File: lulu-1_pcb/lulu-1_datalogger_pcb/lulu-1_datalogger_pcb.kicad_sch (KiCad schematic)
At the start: 38 parts, among them J1 B2B-XH-A, J2 SBH11-PBPC-D10-ST-BK, J3 MEM2067-02-180-00-A_REVB, SW1 SW_Nidec_CAS-120A1, U1 STM32F401RETx, U2 BAT54LT1G, U3 LP3982ILD-3.3, U4 BMP280, U5 MPU-6050, U6 W25Q16JVSS, Y1 25 Mhz, Y2 32 Khz

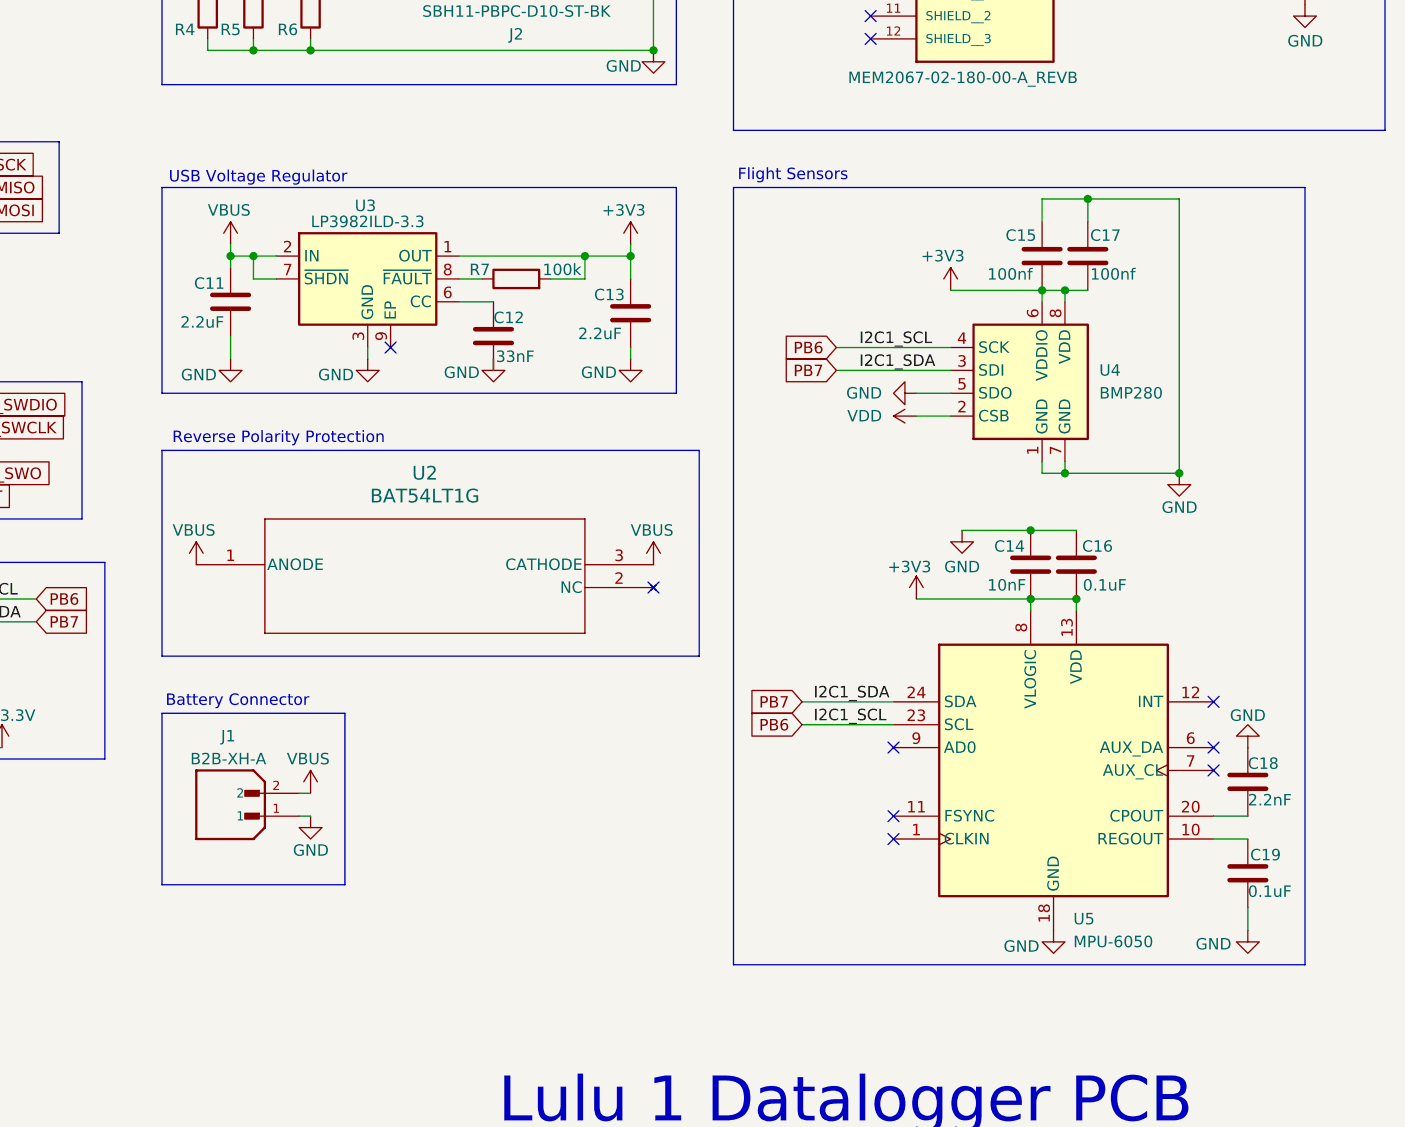
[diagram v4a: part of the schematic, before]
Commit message: added continuity LED to voltage regulator output
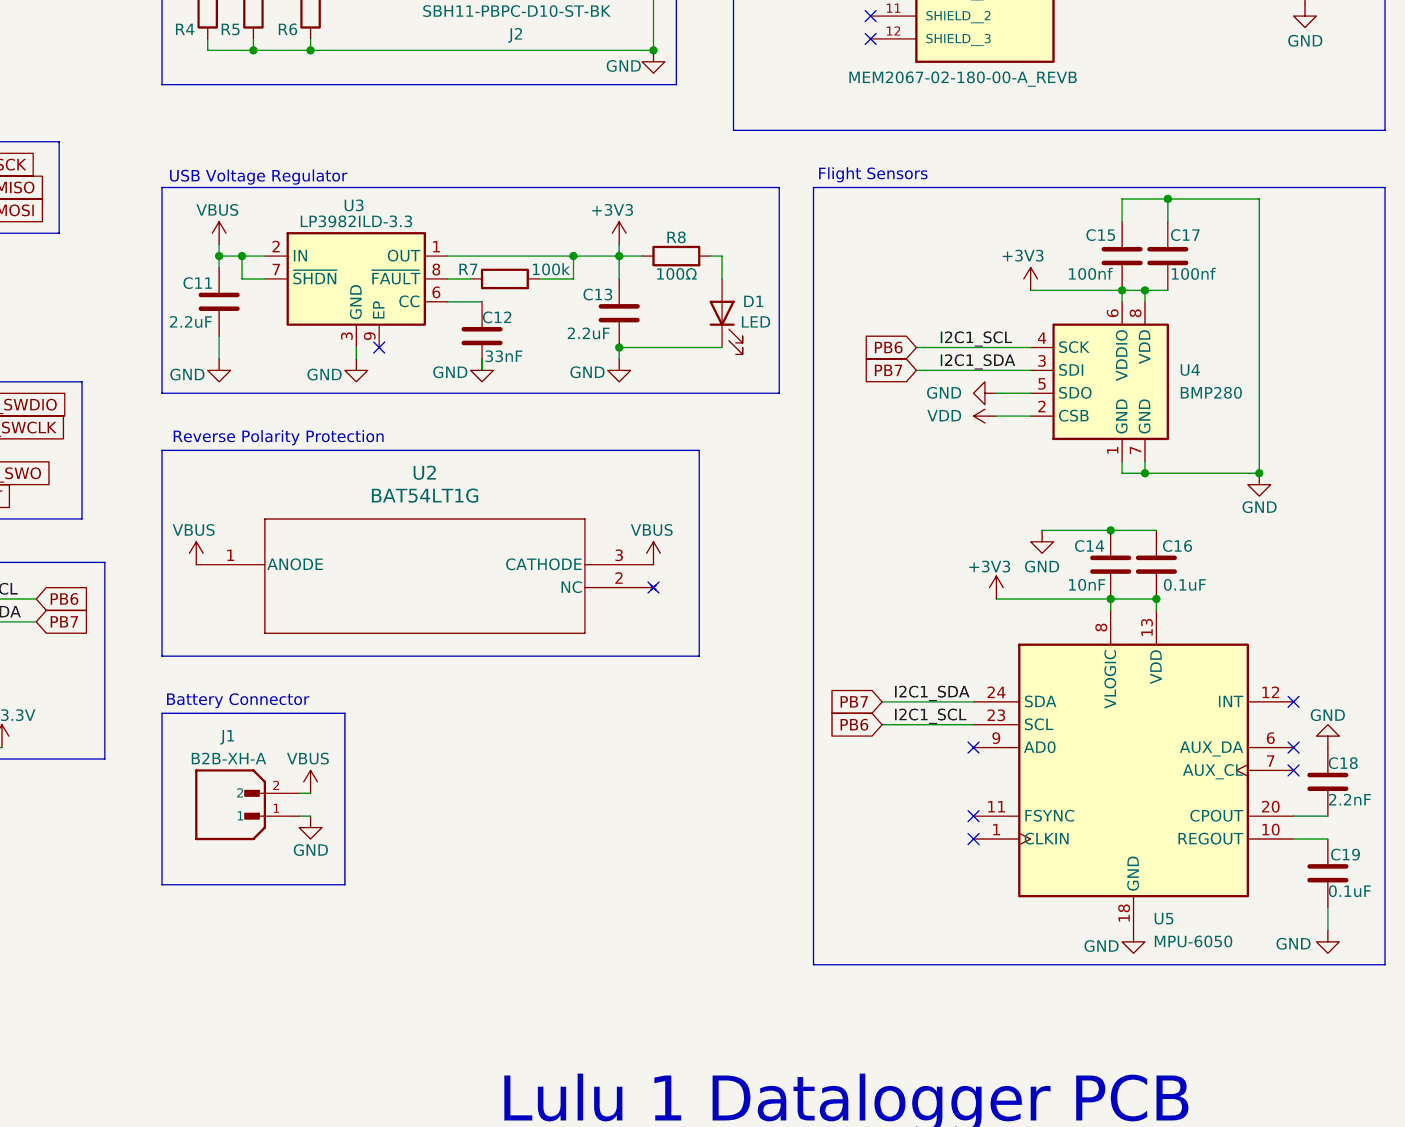
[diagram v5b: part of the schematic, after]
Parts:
- added D1: LED, symbol Device:LED
- added R8: 100Ω, symbol Device:R
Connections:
- net +3V3: now also R8.1
- net GND: now also D1.1 (K)
- new net: D1.2 (A), R8.2
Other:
- moved on the sheet: C11, C12, C13, C14, C15, C16, C17, C18, C19, R7, U3, U4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

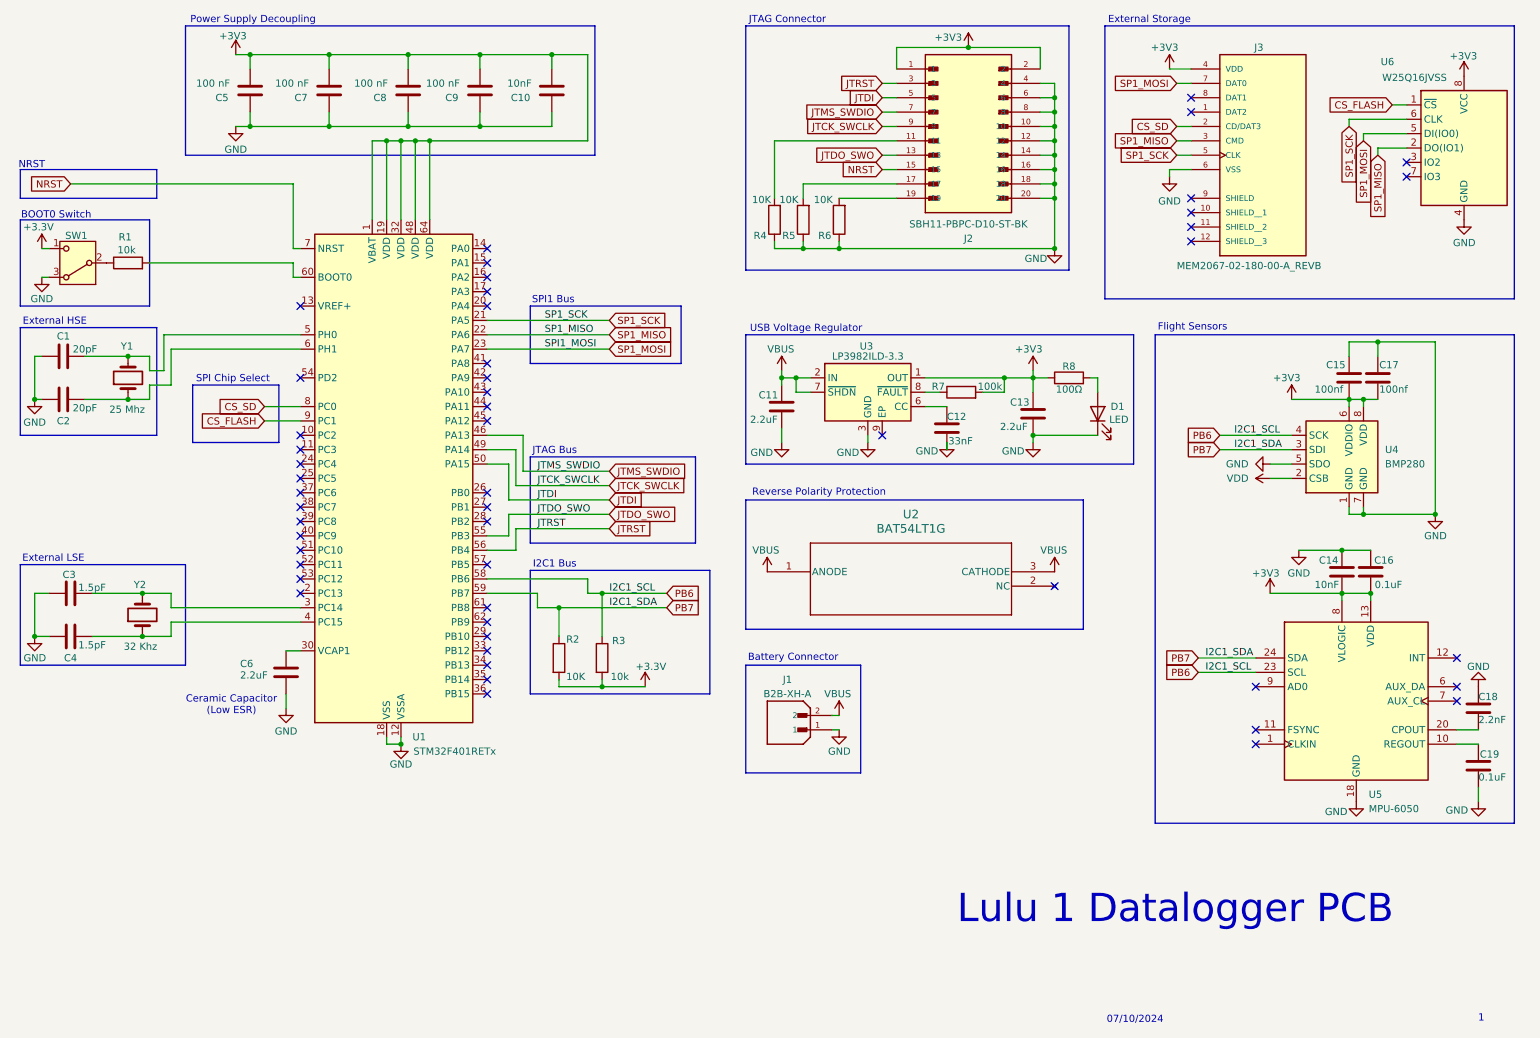
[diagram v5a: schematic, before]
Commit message: added programmable LEDs and buzzer to schematic and to .ioc file
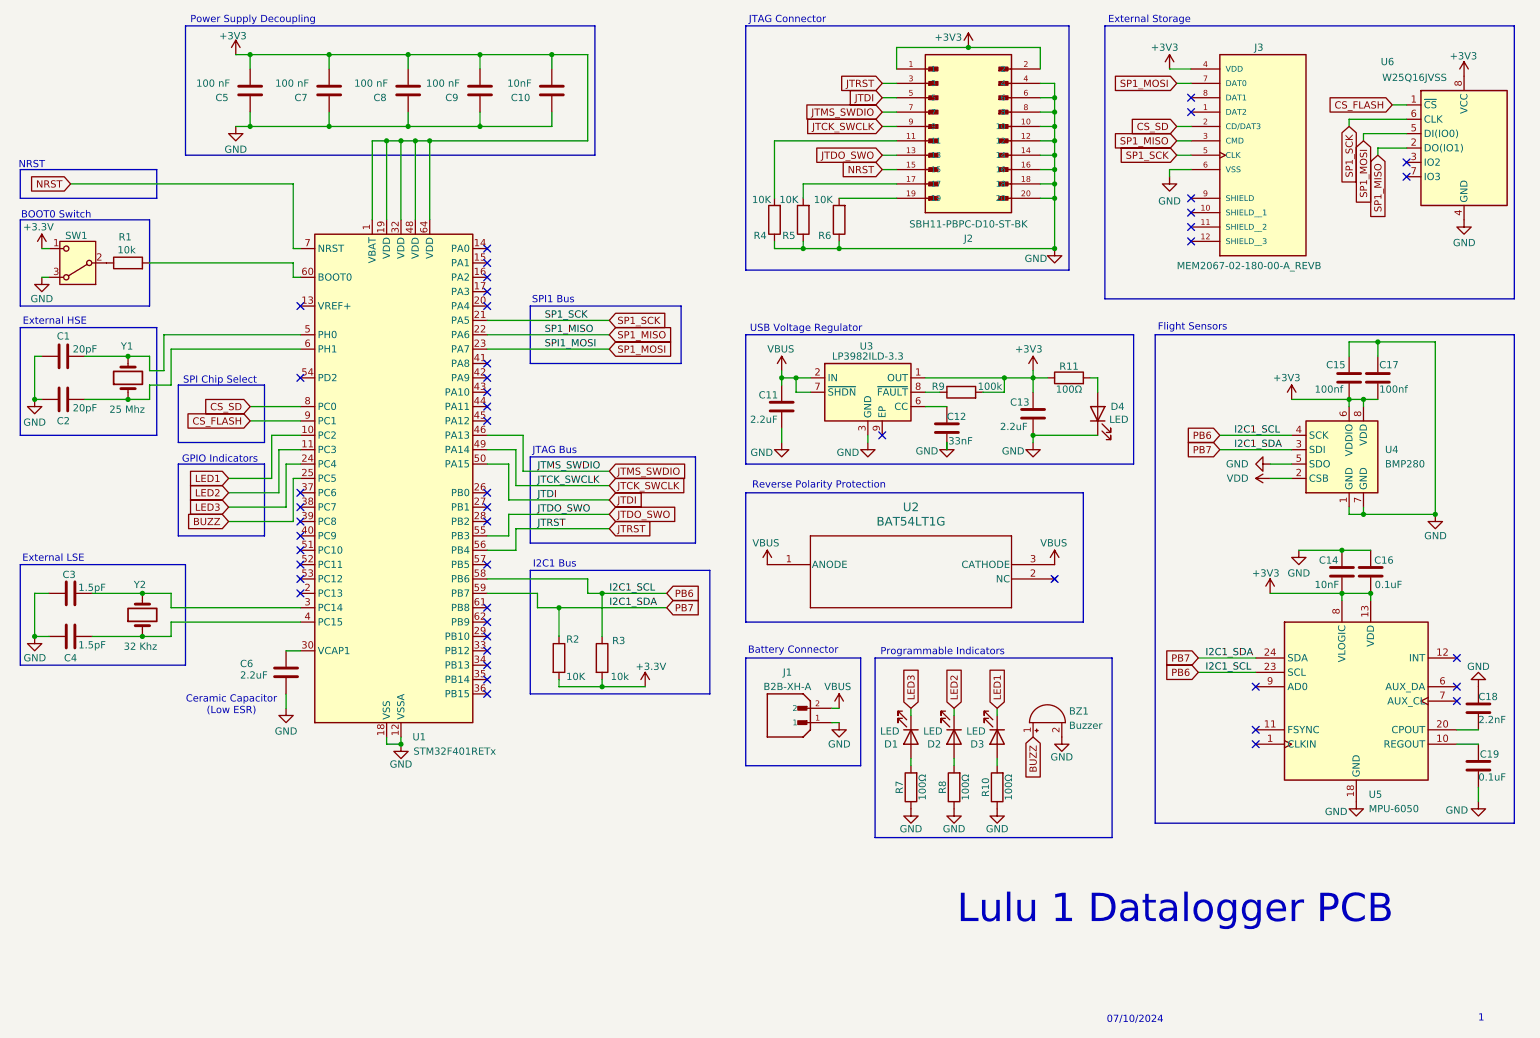
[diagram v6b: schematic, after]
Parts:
- added BZ1: Buzzer, symbol Device:Buzzer
- added D1, D2, D3: LED, symbol Device:LED
- added R10, R7, R8: 100Ω, symbol Device:R
- renumbered D1 to D4, R8 to R11, R7 to R9
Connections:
- net GND: now also BZ1.2 (-), R10.1, R7.1, R8.1
- net LED1: now reaches U1.10 (PC2)
- net LED1: now also D3.1 (K)
- net LED2: now reaches U1.11 (PC3)
- net LED2: now also D2.1 (K)
- net LED3: now reaches U1.24 (PC4)
- net LED3: now also D1.1 (K)
- net BUZZ: now reaches U1.25 (PC5)
- net BUZZ: now also BZ1.1 (+)
- new net: D2.2 (A), R8.2
- new net: D3.2 (A), R10.2
- new net: D1.2 (A), R7.2
- no-connect marks 51 -> 47
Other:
- note added: "GPIO Indicators"
- note added: "Programmable Indicators"
- moved on the sheet: J1, U2

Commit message: assigned footprints to indictors
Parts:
- BZ1: footprint (none) -> AT_1224_TWT_5V_2_R:XDCR_AT-1224-TWT-5V-2-R
- D1, D2, D3: footprint (none) -> 151031VS06000:WL-TMRC_3MM
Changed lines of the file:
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@@
 			)
 		)
-		(property "Footprint" ""
+		(property "Footprint" "AT_1224_TWT_5V_2_R:XDCR_AT-1224-TWT-5V-2-R"
 			(at 195.58 141.605 90)
 			(effects
@@
 			)
 		)
-		(property "Footprint" ""
+		(property "Footprint" "151031VS06000:WL-TMRC_3MM"
 			(at 189.23 143.51 0)
 			(effects
@@
 			)
 		)
-		(property "Footprint" ""
+		(property "Footprint" "151031VS06000:WL-TMRC_3MM"
 			(at 181.61 143.51 0)
 			(effects
@@
 			)
 		)
-		(property "Footprint" ""
+		(property "Footprint" "151031VS06000:WL-TMRC_3MM"
 			(at 173.99 143.51 0)
 			(effects

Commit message: assigned footprint to continuity led
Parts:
- D4: footprint (none) -> 151031VS06000:WL-TMRC_3MM
- R10, R11, R7, R8: footprint (none) -> Resistor_SMD:R_0805_2012Metric_Pad1.20x1.40mm_HandSolder
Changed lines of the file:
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@@
 			)
 		)
-		(property "Footprint" ""
+		(property "Footprint" "151031VS06000:WL-TMRC_3MM"
 			(at 207.01 86.36 0)
 			(effects
@@
 			)
 		)
-		(property "Footprint" ""
+		(property "Footprint" "Resistor_SMD:R_0805_2012Metric_Pad1.20x1.40mm_HandSolder"
 			(at 183.388 152.4 90)
 			(effects
@@
 			)
 		)
-		(property "Footprint" ""
+		(property "Footprint" "Resistor_SMD:R_0805_2012Metric_Pad1.20x1.40mm_HandSolder"
 			(at 175.768 152.4 90)
 			(effects
@@
 			)
 		)
-		(property "Footprint" ""
+		(property "Footprint" "Resistor_SMD:R_0805_2012Metric_Pad1.20x1.40mm_HandSolder"
 			(at 191.008 152.4 90)
 			(effects
@@
 			)
 		)
-		(property "Footprint" ""
+		(property "Footprint" "Resistor_SMD:R_0805_2012Metric_Pad1.20x1.40mm_HandSolder"
 			(at 201.93 81.788 90)
 			(effects
